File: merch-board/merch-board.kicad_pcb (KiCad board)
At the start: 2 copper layers, 86 x 54 mm, 90 parts, among them J1 Piano pads, P1 USB_C_Plug, SW1 BOOTSEL, SW2 RESET, SW3 OCT_DOWN, SW4 OCT_UP, SW5 TONE_SEL, U1 NCP1117-3.3_SOT223, U2 W25Q128JVS, U3 RP2040, U4 PCM5100A, U5 TPA6211A1DGN, U6 CY8CMBR3116, Y1 ABM8-272-T3

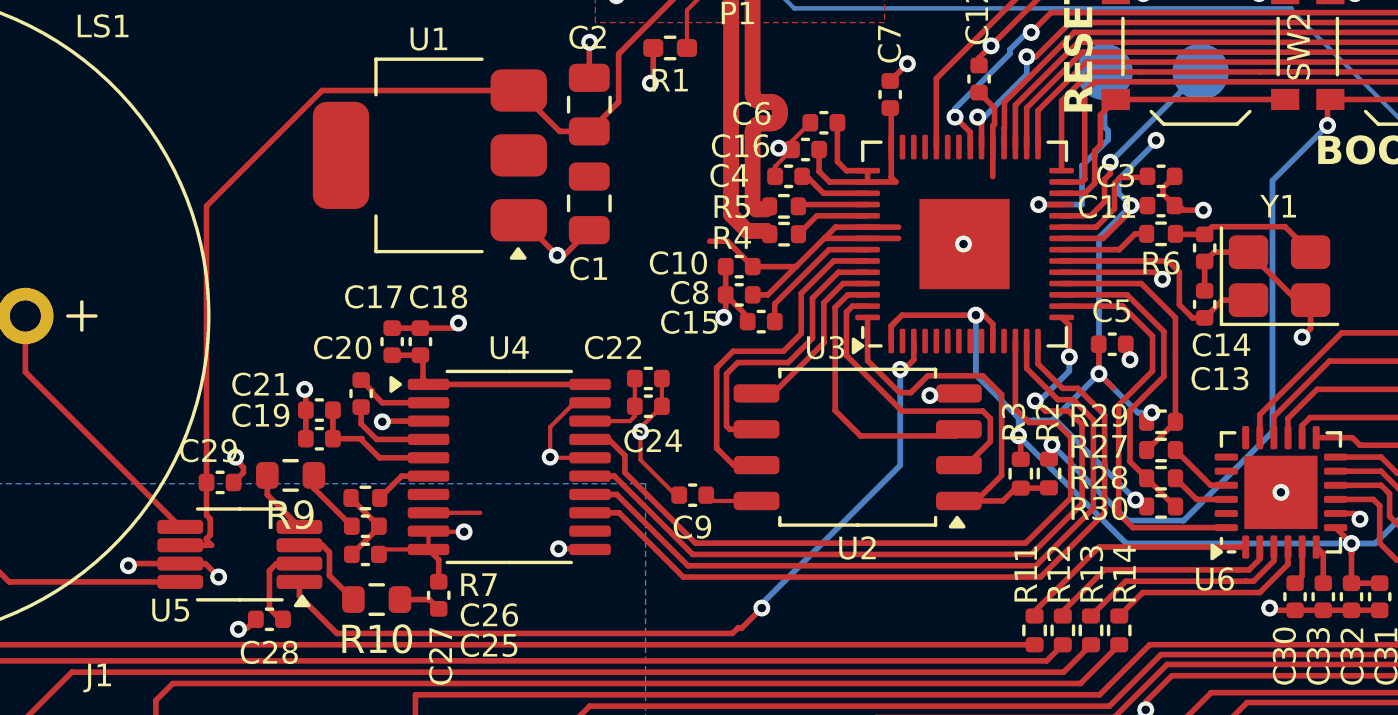
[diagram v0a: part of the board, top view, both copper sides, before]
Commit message: Swap I2C pins around and connect 1v1 output to input
* I2C1 pins 14 and 15 have fixed roles
* 1v1 regulator output from rp2040 is not internally connected to DVDD input
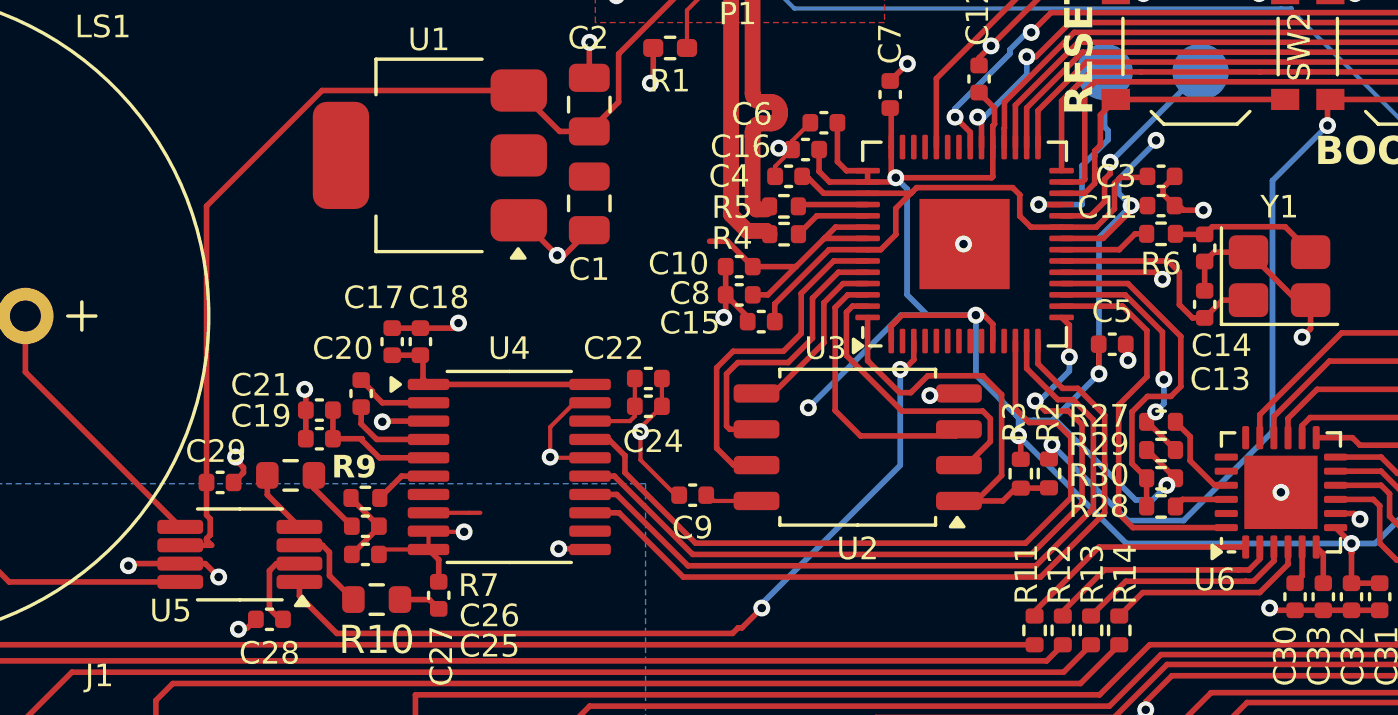
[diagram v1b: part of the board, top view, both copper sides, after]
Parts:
- RV1: value R_Potentiometer -> RK10JR010H
- moved R27 1.00 mm to (165.0, 86.5)
- moved R28 1.00 mm to (165.0, 89.5)
- moved R29 1.00 mm to (165.0, 87.5)
- moved R30 1.00 mm to (165.0, 88.5), turned to 180 degrees
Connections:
- U3 pad 17: /Touch/SCL -> /Touch/SDA
- U3 pad 18: /Touch/SDA -> /Touch/SCL
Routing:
- net +3V3: track 101.5 -> 116.2 mm, vias 8 -> 9
- net +1V1: track 11.6 -> 22.6 mm
- net /Touch/SCL: track 11.5 -> 12.5 mm
- net Net-(U6-SDA): track 2.32 -> 3.24 mm
- net /Touch/SDA: track 9.66 -> 9.01 mm, vias 0 -> 2

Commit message: Update back silkscreen
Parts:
- removed the REF** at (183.5, 104.6)
- added REF**: OSHW-Logo_7.5x8mm_SilkScreen, Symbol:OSHW-Logo_7.5x8mm_SilkScreen, B.Cu at (184.3, 103.9)
- moved REF** 13.2 mm to (157.8, 114.9)
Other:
- board text added: "Design @kaine119 Art @roll4.dan.mage"
- board text removed: "Design @kaine119"
